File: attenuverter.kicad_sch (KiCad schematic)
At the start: 15 parts

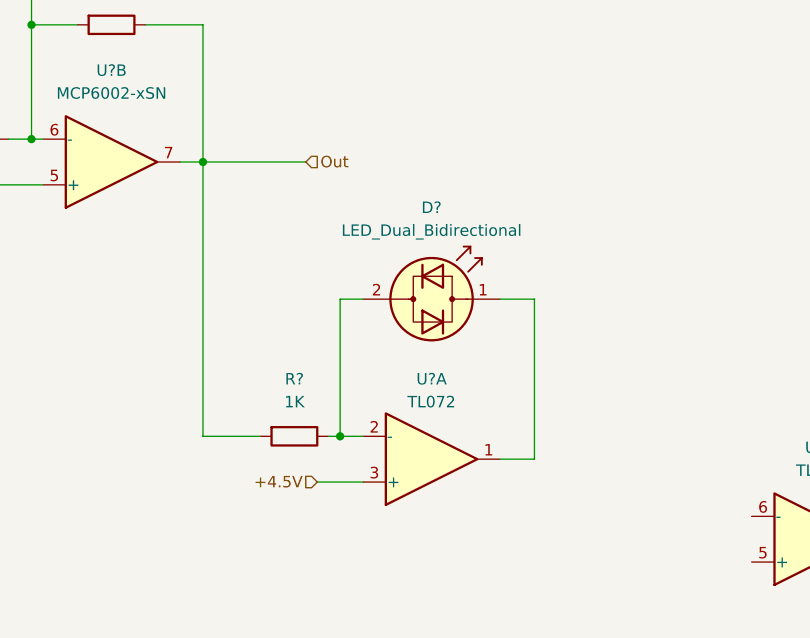
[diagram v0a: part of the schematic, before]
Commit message: Fix: Raise LED driver input impedance
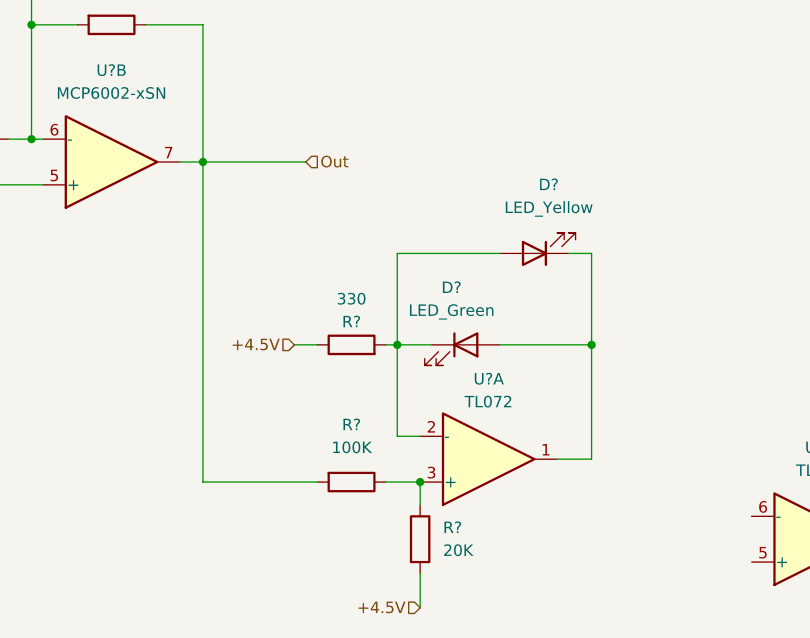
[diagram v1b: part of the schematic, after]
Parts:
- removed D?: LED_Dual_Bidirectional, symbol Device:LED_Dual_Bidirectional
- added D?: LED_Green, symbol Device:LED
- added D?: LED_Yellow, symbol Device:LED
- added R?: 20K, symbol Device:R
- added R?: 330, symbol Device:R
- R?: value 1K -> 100K
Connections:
- net +4.5V: now also R?.1, R?.2; no longer U?.3 (+)
- net at U?.1: now also D?.1 (K), D?.2 (A)
- net at R?.1: now also U?.3 (+), R?.1; no longer U?.2 (-)
- new net: D?.1 (K), D?.2 (A), R?.2, U?.2 (-)
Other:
- moved on the sheet: R?, U?A
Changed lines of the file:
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@@
   (junction (at 134.62 68.58) (diameter 0) (color 0 0 0 0)
   )
-  (junction (at 149.86 99.06) (diameter 0) (color 0 0 0 0)
+  (junction (at 156.21 88.9) (diameter 0) (color 0 0 0 0)
+  )
+  (junction (at 177.8 88.9) (diameter 0) (color 0 0 0 0)
+  )
+  (junction (at 158.75 104.14) (diameter 0) (color 0 0 0 0)
   )
   (junction (at 93.98 66.04) (diameter 0) (color 0 0 0 0)
@@
     (stroke (width 0) (type default) (color 0 0 0 0))
   )
+  (wire (pts (xy 156.21 88.9) (xy 154.94 88.9))
+    (stroke (width 0) (type default) (color 0 0 0 0))
+  )
   (wire (pts (xy 134.62 68.58) (xy 132.08 68.58))
     (stroke (width 0) (type default) (color 0 0 0 0))
@@
     (stroke (width 0) (type default) (color 0 0 0 0))
   )
-  (wire (pts (xy 149.86 83.82) (xy 149.86 99.06))
+  (wire (pts (xy 156.21 88.9) (xy 156.21 99.06))
     (stroke (width 0) (type default) (color 0 0 0 0))
   )
@@
     (stroke (width 0) (type default) (color 0 0 0 0))
   )
-  (wire (pts (xy 167.64 83.82) (xy 171.45 83.82))
+  (wire (pts (xy 167.64 88.9) (xy 177.8 88.9))
     (stroke (width 0) (type default) (color 0 0 0 0))
   )
@@
     (stroke (width 0) (type default) (color 0 0 0 0))
   )
+  (wire (pts (xy 158.75 104.14) (xy 158.75 106.68))
+    (stroke (width 0) (type default) (color 0 0 0 0))
+  )
   (wire (pts (xy 120.65 53.34) (xy 115.57 53.34))
     (stroke (width 0) (type default) (color 0 0 0 0))
@@
     (stroke (width 0) (type default) (color 0 0 0 0))
   )
-  (wire (pts (xy 171.45 83.82) (xy 171.45 101.6))
+  (wire (pts (xy 158.75 114.3) (xy 158.75 118.11))
+    (stroke (width 0) (type default) (color 0 0 0 0))
+  )
+  (wire (pts (xy 177.8 88.9) (xy 177.8 101.6))
+    (stroke (width 0) (type default) (color 0 0 0 0))
+  )
+  (wire (pts (xy 156.21 78.74) (xy 167.64 78.74))
     (stroke (width 0) (type default) (color 0 0 0 0))
   )
@@
     (stroke (width 0) (type default) (color 0 0 0 0))
   )
-  (wire (pts (xy 134.62 99.06) (xy 134.62 68.58))
+  (wire (pts (xy 134.62 68.58) (xy 134.62 104.14))
     (stroke (width 0) (type default) (color 0 0 0 0))
   )
@@
     (stroke (width 0) (type default) (color 0 0 0 0))
   )
+  (wire (pts (xy 156.21 88.9) (xy 156.21 78.74))
+    (stroke (width 0) (type default) (color 0 0 0 0))
+  )
   (wire (pts (xy 115.57 53.34) (xy 115.57 66.04))
     (stroke (width 0) (type default) (color 0 0 0 0))
   )
-  (wire (pts (xy 152.4 83.82) (xy 149.86 83.82))
-    (stroke (width 0) (type default) (color 0 0 0 0))
-  )
-  (wire (pts (xy 149.86 99.06) (xy 152.4 99.06))
+  (wire (pts (xy 177.8 78.74) (xy 177.8 88.9))
+    (stroke (width 0) (type default) (color 0 0 0 0))
+  )
+  (wire (pts (xy 154.94 104.14) (xy 158.75 104.14))
+    (stroke (width 0) (type default) (color 0 0 0 0))
+  )
+  (wire (pts (xy 156.21 88.9) (xy 160.02 88.9))
+    (stroke (width 0) (type default) (color 0 0 0 0))
+  )
+  (wire (pts (xy 156.21 99.06) (xy 158.75 99.06))
     (stroke (width 0) (type default) (color 0 0 0 0))
   )
@@
     (stroke (width 0) (type default) (color 0 0 0 0))
   )
-  (wire (pts (xy 147.32 104.14) (xy 152.4 104.14))
+  (wire (pts (xy 147.32 104.14) (xy 134.62 104.14))
     (stroke (width 0) (type default) (color 0 0 0 0))
   )
@@
     (stroke (width 0) (type default) (color 0 0 0 0))
   )
-  (wire (pts (xy 148.59 99.06) (xy 149.86 99.06))
-    (stroke (width 0) (type default) (color 0 0 0 0))
-  )
   (wire (pts (xy 87.63 53.34) (xy 93.98 53.34))
     (stroke (width 0) (type default) (color 0 0 0 0))
   )
-  (wire (pts (xy 171.45 101.6) (xy 167.64 101.6))
-    (stroke (width 0) (type default) (color 0 0 0 0))
-  )
-  (wire (pts (xy 140.97 99.06) (xy 134.62 99.06))
+  (wire (pts (xy 177.8 101.6) (xy 173.99 101.6))
+    (stroke (width 0) (type default) (color 0 0 0 0))
+  )
+  (wire (pts (xy 175.26 78.74) (xy 177.8 78.74))
     (stroke (width 0) (type default) (color 0 0 0 0))
   )
   (wire (pts (xy 50.8 77.47) (xy 50.8 83.82))
+    (stroke (width 0) (type default) (color 0 0 0 0))
+  )
+  (wire (pts (xy 147.32 88.9) (xy 144.78 88.9))
     (stroke (width 0) (type default) (color 0 0 0 0))
   )
@@
     (effects (font (size 1.27 1.27)) (justify left bottom))
   )
-  (hierarchical_label "+4.5V" (shape input) (at 147.32 104.14 180)
+  (hierarchical_label "+4.5V" (shape input) (at 144.78 88.9 180)
     (effects (font (size 1.27 1.27)) (justify right))
   )
   (hierarchical_label "+4.5V" (shape input) (at 50.8 83.82 180)
+    (effects (font (size 1.27 1.27)) (justify right))
+  )
+  (hierarchical_label "+4.5V" (shape input) (at 158.75 118.11 180)
     (effects (font (size 1.27 1.27)) (justify right))
   )
@@
   (hierarchical_label "+9V" (shape input) (at 93.98 30.48 90)
     (effects (font (size 1.27 1.27)) (justify left))
+  )
+  (symbol (lib_id "Device:R") (at 158.75 110.49 0) (unit 1)
+    (in_bom yes) (on_board yes) (fields_autoplaced)
+    (property "Reference" "R?" (id 0) (at 161.29 109.2199 0)
+      (effects (font (size 1.27 1.27)) (justify left))
+    )
+    (property "Value" "20K" (id 1) (at 161.29 111.7599 0)
+      (effects (font (size 1.27 1.27)) (justify left))
+    )
+    (property "Footprint" "" (id 2) (at 156.972 110.49 90)
+      (effects (font (size 1.27 1.27)) hide)
+    )
+    (property "Datasheet" "~" (id 3) (at 158.75 110.49 0)
+      (effects (font (size 1.27 1.27)) hide)
+    )
+    (pin "1")
+    (pin "2")
+  )
+  (symbol (lib_id "Device:LED") (at 163.83 88.9 0) (unit 1)
+    (in_bom yes) (on_board yes) (fields_autoplaced)
+    (property "Reference" "D?" (id 0) (at 162.2425 82.55 0))
+    (property "Value" "LED_Green" (id 1) (at 162.2425 85.09 0))
+    (property "Footprint" "" (id 2) (at 163.83 88.9 0)
+      (effects (font (size 1.27 1.27)) hide)
+    )
+    (property "Datasheet" "~" (id 3) (at 163.83 88.9 0)
+      (effects (font (size 1.27 1.27)) hide)
+    )
+    (pin "1")
+    (pin "2")
   )
   (symbol (lib_id "Device:R_Potentiometer") (at 101.6 30.48 270) (unit 1)
@@
     (pin "2")
   )
-  (symbol (lib_id "Device:LED_Dual_Bidirectional") (at 160.02 83.82 0) (unit 1)
-    (in_bom yes) (on_board yes)
-    (property "Reference" "D?" (id 0) (at 160.02 73.66 0))
-    (property "Value" "LED_Dual_Bidirectional" (id 1) (at 160.02 76.2 0))
-    (property "Footprint" "" (id 2) (at 160.02 83.82 0)
-      (effects (font (size 1.27 1.27)) hide)
-    )
-    (property "Datasheet" "~" (id 3) (at 160.02 83.82 0)
-      (effects (font (size 1.27 1.27)) hide)
-    )
-    (pin "1")
-    (pin "2")
-  )
   (symbol (lib_id "Device:R") (at 124.46 53.34 270) (unit 1)
     (in_bom yes) (on_board yes) (fields_autoplaced)
@@
     (pin "8")
   )
-  (symbol (lib_id "Amplifier_Operational:TL072") (at 160.02 101.6 0) (mirror x) (unit 1)
+  (symbol (lib_id "Amplifier_Operational:TL072") (at 166.37 101.6 0) (mirror x) (unit 1)
     (in_bom yes) (on_board yes)
-    (property "Reference" "U?" (id 0) (at 160.02 92.71 0))
-    (property "Value" "TL072" (id 1) (at 160.02 95.25 0))
-    (property "Footprint" "" (id 2) (at 160.02 101.6 0)
-      (effects (font (size 1.27 1.27)) hide)
-    )
-    (property "Datasheet" "http://www.ti.com/lit/ds/symlink/tl071.pdf" (id 3) (at 160.02 101.6 0)
-      (effects (font (size 1.27 1.27)) hide)
-    )
-    (pin "1")
-    (pin "2")
-    (pin "3")
-    (pin "5")
-    (pin "6")
-    (pin "7")
-    (pin "4")
-    (pin "8")
+    (property "Reference" "U?" (id 0) (at 166.37 92.71 0))
+    (property "Value" "TL072" (id 1) (at 166.37 95.25 0))
+    (property "Footprint" "" (id 2) (at 166.37 101.6 0)
+      (effects (font (size 1.27 1.27)) hide)
+    )
+    (property "Datasheet" "http://www.ti.com/lit/ds/symlink/tl071.pdf" (id 3) (at 166.37 101.6 0)
+      (effects (font (size 1.27 1.27)) hide)
+    )
+    (pin "1")
+    (pin "2")
+    (pin "3")
+    (pin "5")
+    (pin "6")
+    (pin "7")
+    (pin "4")
+    (pin "8")
+  )
+  (symbol (lib_id "Device:LED") (at 171.45 78.74 180) (unit 1)
+    (in_bom yes) (on_board yes) (fields_autoplaced)
+    (property "Reference" "D?" (id 0) (at 173.0375 71.12 0))
+    (property "Value" "LED_Yellow" (id 1) (at 173.0375 73.66 0))
+    (property "Footprint" "" (id 2) (at 171.45 78.74 0)
+      (effects (font (size 1.27 1.27)) hide)
+    )
+    (property "Datasheet" "~" (id 3) (at 171.45 78.74 0)
+      (effects (font (size 1.27 1.27)) hide)
+    )
+    (pin "1")
+    (pin "2")
   )
   (symbol (lib_id "Device:R") (at 109.22 66.04 270) (unit 1)
@@
     (pin "8")
   )
-  (symbol (lib_id "Device:R") (at 144.78 99.06 270) (unit 1)
-    (in_bom yes) (on_board yes) (fields_autoplaced)
-    (property "Reference" "R?" (id 0) (at 144.78 92.71 90))
-    (property "Value" "1K" (id 1) (at 144.78 95.25 90))
-    (property "Footprint" "" (id 2) (at 144.78 97.282 90)
-      (effects (font (size 1.27 1.27)) hide)
-    )
-    (property "Datasheet" "~" (id 3) (at 144.78 99.06 0)
-      (effects (font (size 1.27 1.27)) hide)
-    )
+  (symbol (lib_id "Device:R") (at 151.13 104.14 270) (unit 1)
+    (in_bom yes) (on_board yes) (fields_autoplaced)
+    (property "Reference" "R?" (id 0) (at 151.13 97.79 90))
+    (property "Value" "100K" (id 1) (at 151.13 100.33 90))
+    (property "Footprint" "" (id 2) (at 151.13 102.362 90)
+      (effects (font (size 1.27 1.27)) hide)
+    )
+    (property "Datasheet" "~" (id 3) (at 151.13 104.14 0)
+      (effects (font (size 1.27 1.27)) hide)
+    )
+    (pin "1")
+    (pin "2")
+  )
+  (symbol (lib_id "Device:R") (at 151.13 88.9 90) (unit 1)
+    (in_bom yes) (on_board yes)
+    (property "Reference" "R?" (id 0) (at 151.13 86.36 90))
+    (property "Value" "330" (id 1) (at 151.13 83.82 90))
+    (property "Footprint" "" (id 2) (at 151.13 90.678 90)
+      (effects (font (size 1.27 1.27)) hide)
+    )
+    (property "Datasheet" "~" (id 3) (at 151.13 88.9 0)
+      (effects (font (size 1.27 1.27)) hide)
+    )

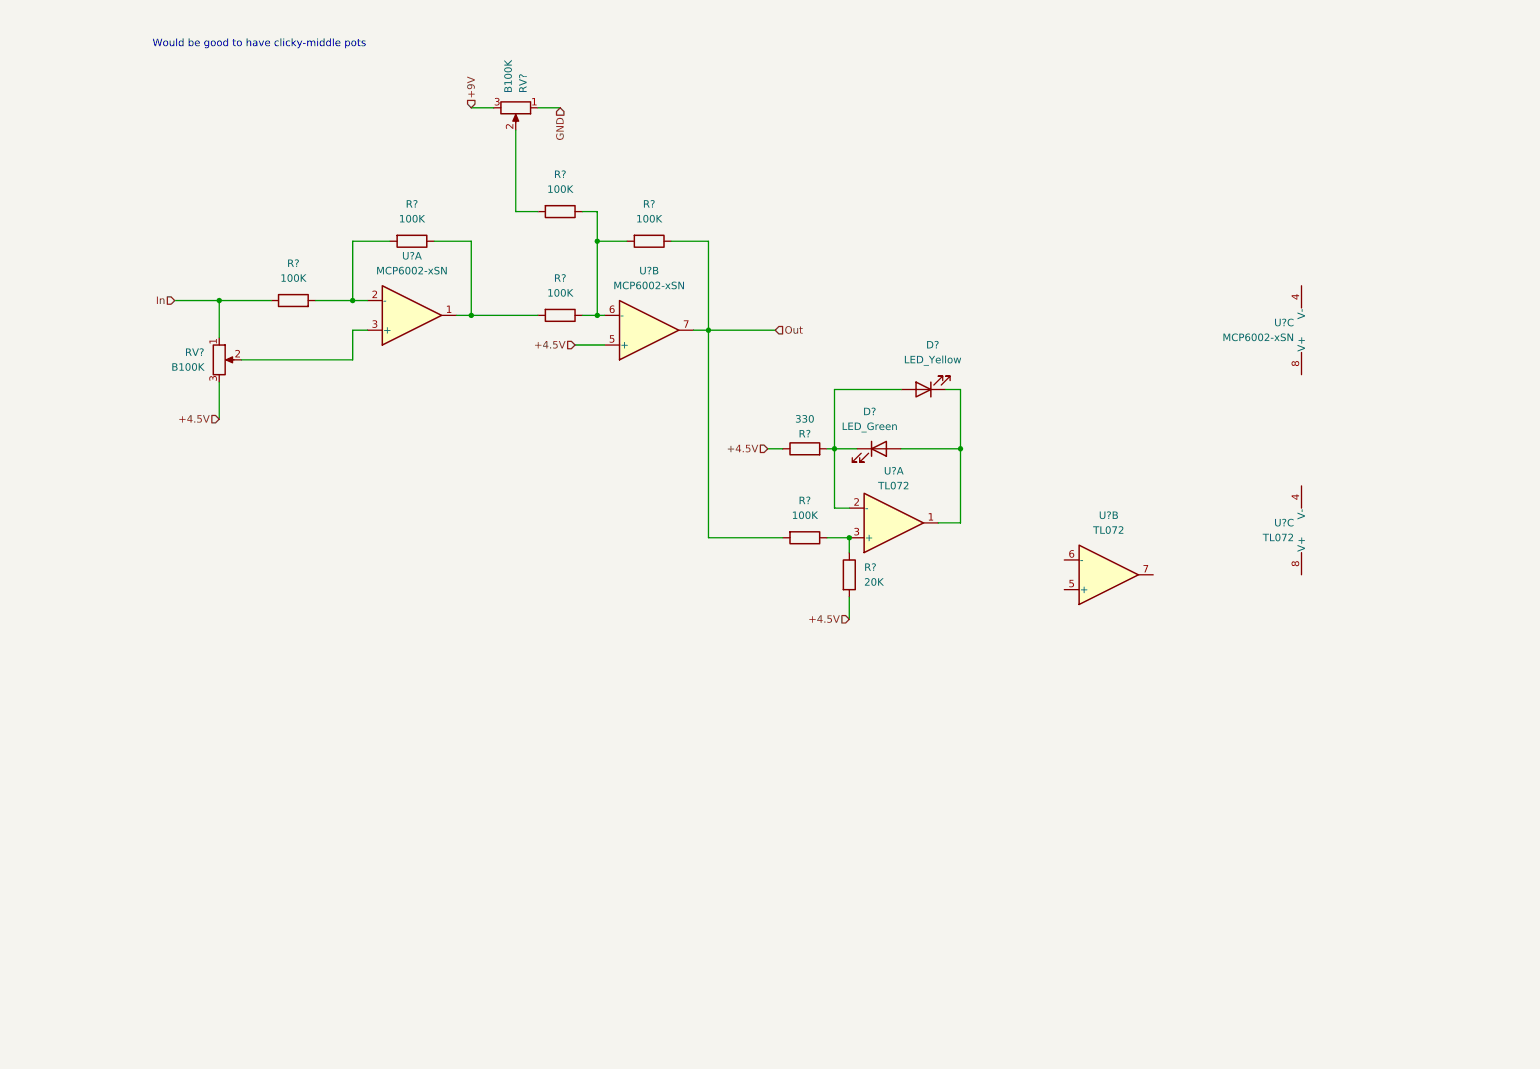
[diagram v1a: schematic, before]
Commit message: Add circuitjs for verified blocks
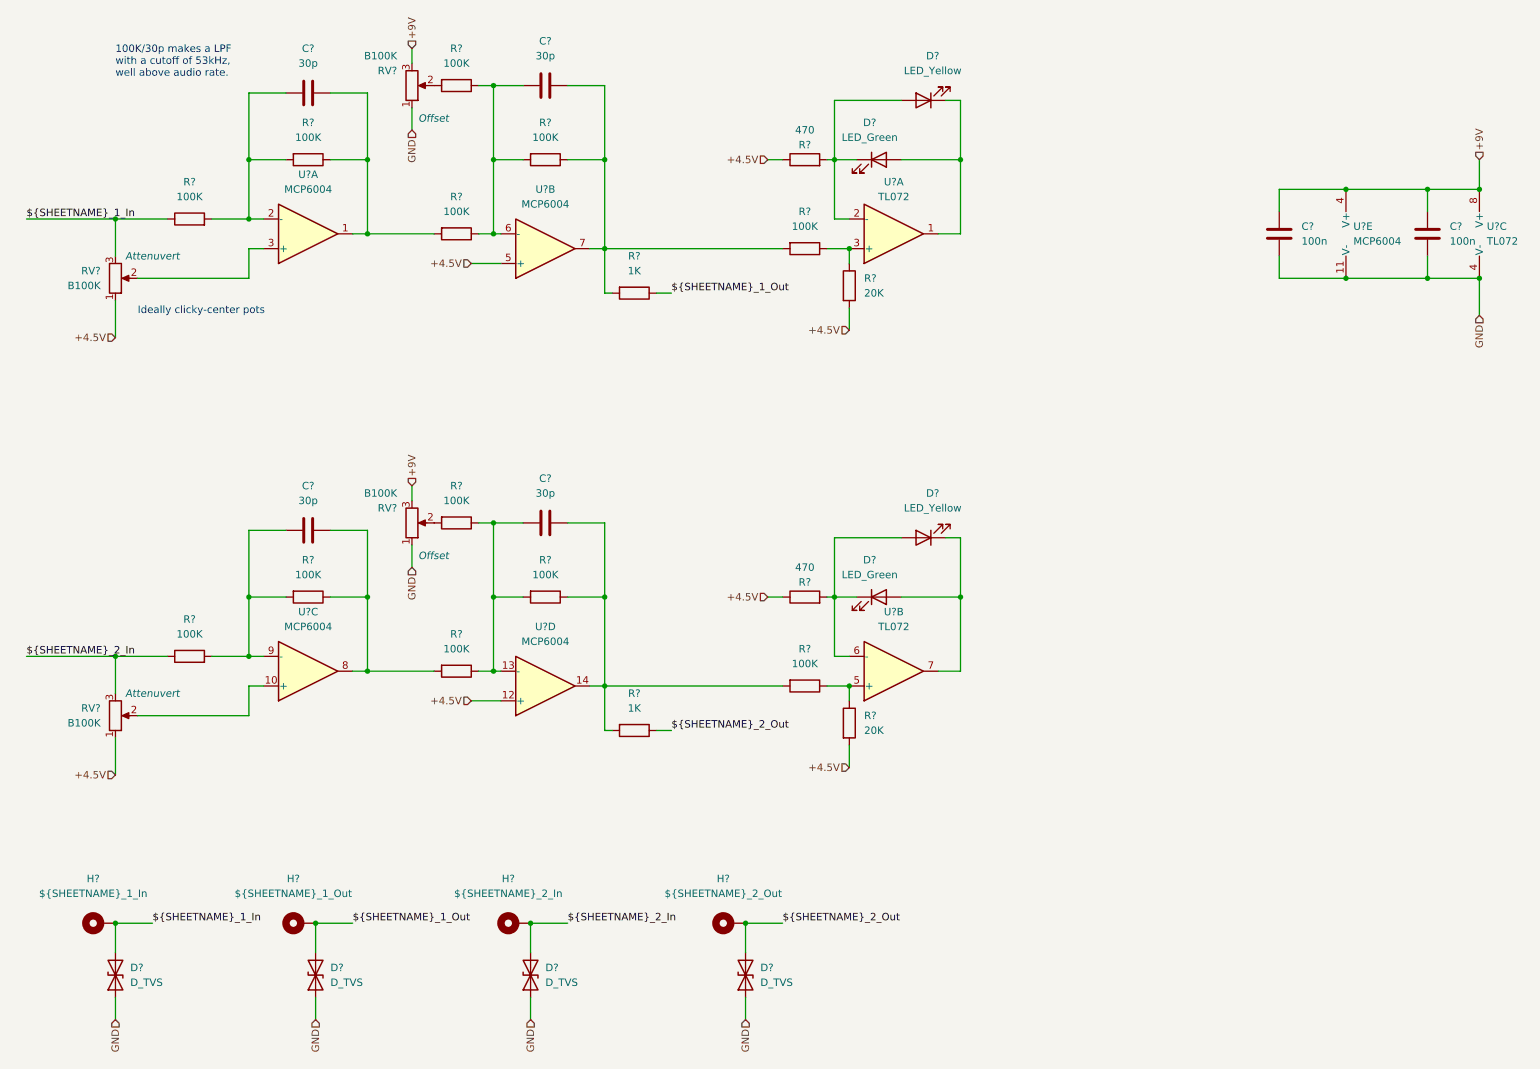
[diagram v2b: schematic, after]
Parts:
- removed U? (x3): MCP6002-xSN, symbol Amplifier_Operational:MCP6002-xSN
- added C? (x4): 30p, symbol Device:C
- added C? (x2): 100n, symbol Device:C
- added D? (x4): D_TVS, symbol Device:D_TVS
- added D?: LED_Green, symbol Device:LED
- added D?: LED_Yellow, symbol Device:LED
- added H?: ${SHEETNAME}_1_In, symbol Mechanical:MountingHole_Pad
- added H?: ${SHEETNAME}_2_Out, symbol Mechanical:MountingHole_Pad
- added H?: ${SHEETNAME}_2_In, symbol Mechanical:MountingHole_Pad
- added H?: ${SHEETNAME}_1_Out, symbol Mechanical:MountingHole_Pad
- added R? (x6): 100K, symbol Device:R
- added R? (x2): 1K, symbol Device:R
- added R?: 20K, symbol Device:R
- added R?: 470, symbol Device:R
- added RV? (x2): B100K, symbol Device:R_Potentiometer
- added U? (x5): MCP6004, symbol Amplifier_Operational:MCP6004
- R?: value 330 -> 470
- RV?: Role (none) -> Offset
- RV?: Role (none) -> Attenuvert
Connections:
- net +4.5V: now also RV?.1, R?.1, R?.2, RV?.1, U?.12 (+), U?.5 (+); no longer RV?.3
- net +9V: now also U?.8 (V+), C?.1, C?.1, RV?.3, U?.4 (V+)
- net GND: now also U?.4 (V-), C?.2, C?.2, D?.1 (A1), D?.1 (A1), D?.1 (A1), D?.1 (A1), RV?.1, U?.11 (V-)
- net at R?.1, R?.2: now also C?.2, U?.1
- net at R?.2, R?.2: now also C?.1, U?.2 (-)
- net at RV?.2: now also U?.3 (+)
- net at R?.1, R?.1, R?.2: now also C?.1, U?.6 (-)
- net at U?.5 (+): now also R?.1, R?.1
- net at U?.6 (-): now also D?.1 (K), D?.2 (A), R?.2
- net at U?.7: now also D?.1 (K), D?.2 (A)
- net In renamed ${SHEETNAME}_1_In
- net ${SHEETNAME}_1_In: now also RV?.3, D?.2 (A2), H?.1; no longer RV?.1
- net Out: no longer names the net of R?.1, R?.2
- net Out: now also C?.2, R?.2, U?.7
- new net: C?.2, R?.1, R?.2, R?.2, U?.14
- new net: C?.1, R?.1, R?.1, R?.2, U?.13 (-)
- new net: R?.2, RV?.2
- new net: C?.1, R?.2, R?.2, U?.9 (-)
- new net: C?.2, R?.1, R?.2, U?.8
- new net: RV?.2, U?.10 (+)
- new net ${SHEETNAME}_1_Out: D?.2 (A2), H?.1, R?.1
- new net ${SHEETNAME}_2_In: D?.2 (A2), H?.1, R?.1, RV?.3
- new net ${SHEETNAME}_2_Out: D?.2 (A2), H?.1, R?.1
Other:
- note added: "100K/30p makes a LPF with a cutoff of 53kHz, well above audio rate."
- note added: "Ideally clicky-center pots"
- note removed: "Would be good to have clicky-middle pots"
- moved on the sheet: D?, R?, RV?, U?A, U?B, U?C
